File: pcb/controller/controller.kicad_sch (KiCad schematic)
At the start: 0 parts

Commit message: big components placed
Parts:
- added U1: ESP32-H2, PCM_Espressif:QFN-32-1EP_4x4mm_P0.4mm_EP2.9x2.9mm, symbol Espressif:ESP32-H2
- added U2: LSM6DSM, Package_LGA:LGA-14_3x2.5mm_P0.5mm_LayoutBorder3x4y, symbol Sensor_Motion:LSM6DSM
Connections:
- new net: U2.6 (GND), U2.7 (GND)
- new net: U1.1 (VDD3P3), U1.2 (VDD3P3), U1.27 (VDD3P3), U1.30 (VDD3P3), U1.31 (VDD3P3)

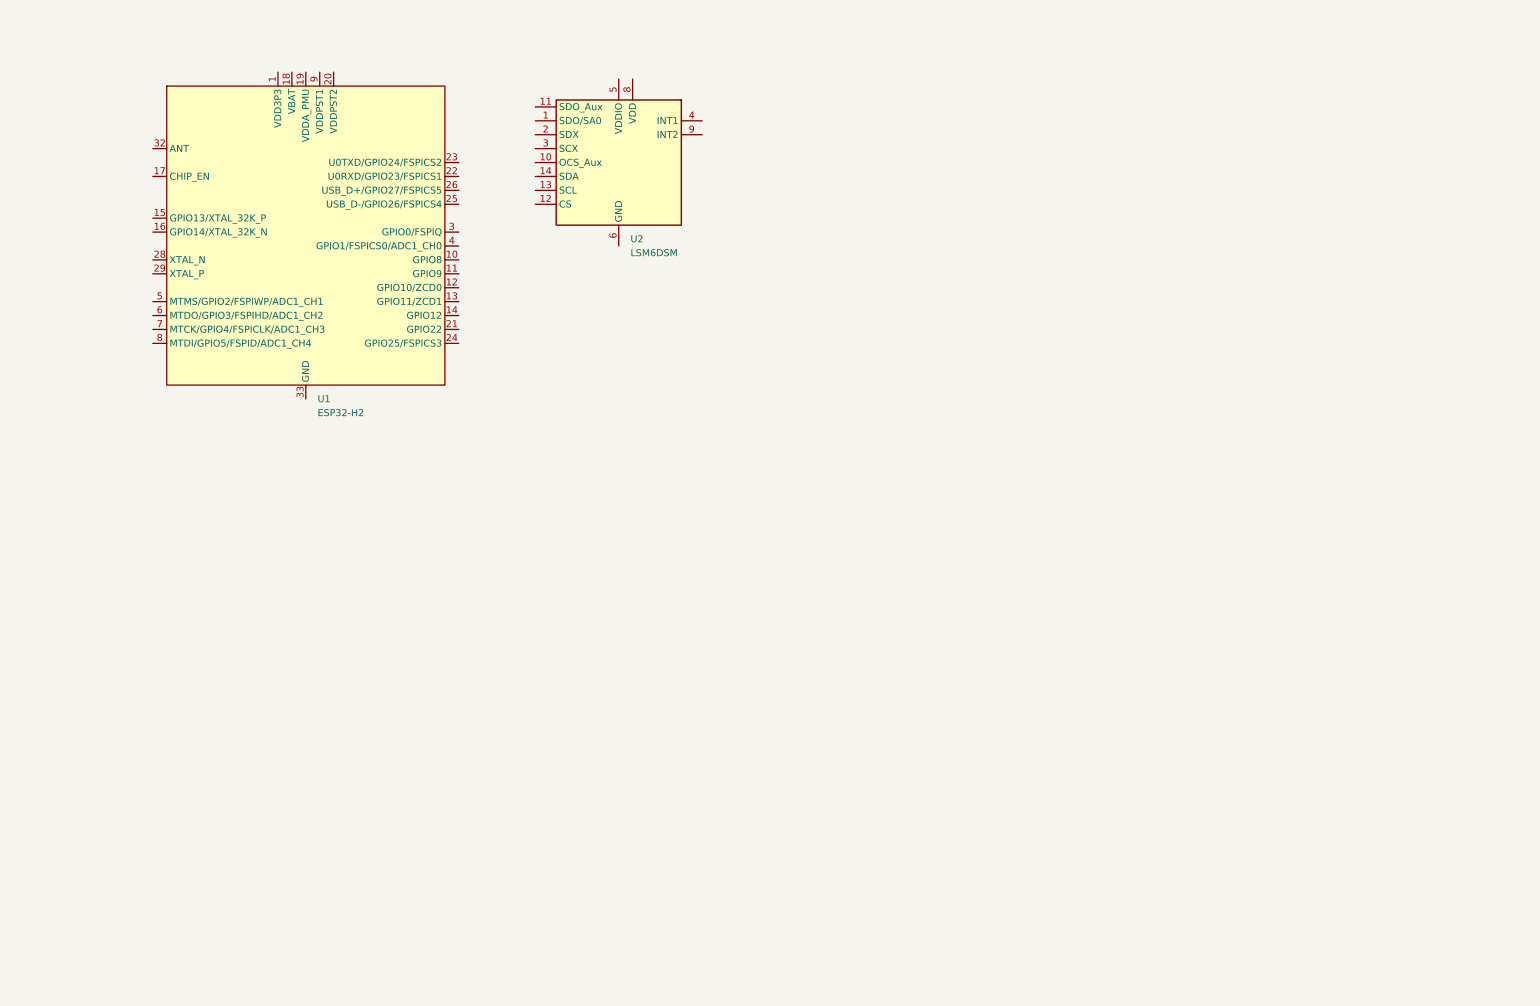
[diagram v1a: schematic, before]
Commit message: copied over wifi board without antenna
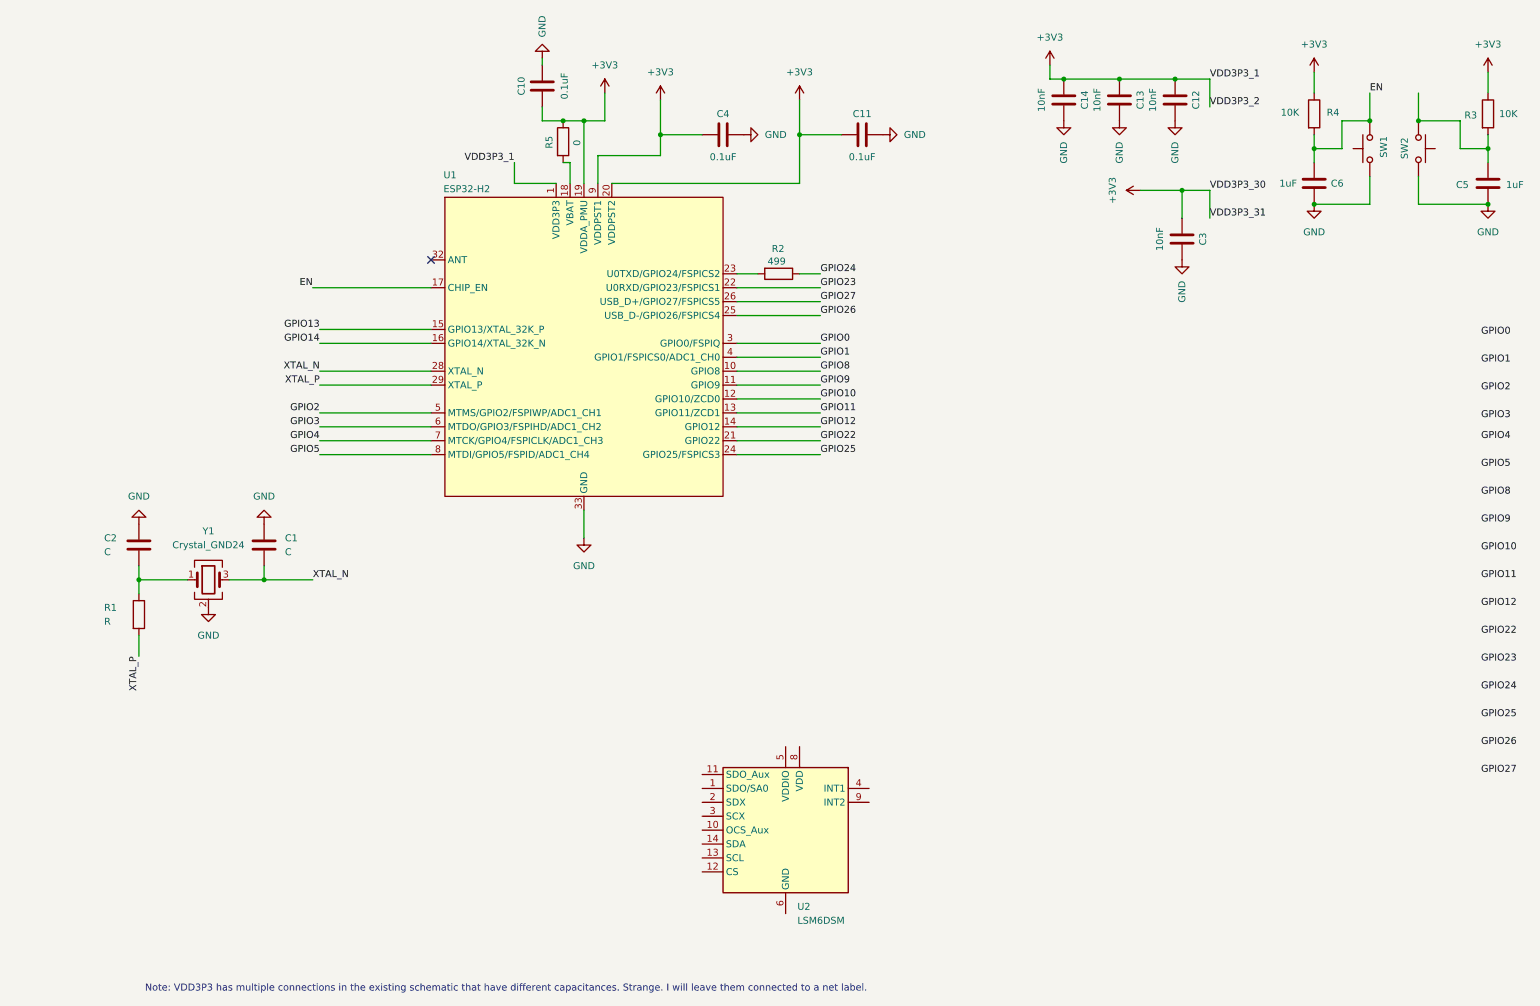
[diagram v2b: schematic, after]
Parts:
- added C1, C2: C, symbol Device:C
- added C10, C11, C4: 0.1uF, symbol Device:C
- added C12, C13, C14, C3: 10nF, symbol Device:C
- added C5, C6: 1uF, symbol Device:C
- added R1: R, symbol Device:R
- added R2: 499, symbol Device:R
- added R3, R4: 10K, symbol Device:R
- added R5: 0, symbol Device:R
- added SW1, SW2: SW_Push, symbol Switch:SW_Push
- added Y1: Crystal_GND24, Crystal:Crystal_SMD_2016-4Pin_2.0x1.6mm, symbol Device:Crystal_GND24
- U1: footprint PCM_Espressif:QFN-32-1EP_4x4mm_P0.4mm_EP2.9x2.9mm -> Espressif:QFN-32-1EP_4x4mm_P0.4mm_EP2.9x2.9mm
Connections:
- net +3V3: now reaches U1.1 (VDD3P3), U1.2 (VDD3P3), U1.27 (VDD3P3), U1.30 (VDD3P3), U1.31 (VDD3P3)
- net +3V3: now also U1.19 (VDDA_PMU), U1.20 (VDDPST2), U1.9 (VDDPST1), C10.2, C11.2, C12.2, C13.2, C14.2, C3.2, C4.2, R3.1, R4.1, R5.1
- net GPIO8: now reaches U1.10 (GPIO8)
- net GPIO9: now reaches U1.11 (GPIO9)
- net GPIO10: now reaches U1.12 (GPIO10/ZCD0)
- net GPIO11: now reaches U1.13 (GPIO11/ZCD1)
- net GPIO12: now reaches U1.14 (GPIO12)
- net GPIO13: now reaches U1.15 (GPIO13/XTAL_32K_P)
- net GPIO14: now reaches U1.16 (GPIO14/XTAL_32K_N)
- net EN: now reaches U1.17 (CHIP_EN)
- net EN: now also C6.1, R4.2, SW1.2
- net at U1.18 (VBAT): now also R5.2
- net GPIO22: now reaches U1.21 (GPIO22)
- net GPIO23: now reaches U1.22 (U0RXD/GPIO23/FSPICS1)
- net at U1.23 (U0TXD/GPIO24/FSPICS2): now also R2.2
- net GPIO25: now reaches U1.24 (GPIO25/FSPICS3)
- net GPIO26: now reaches U1.25 (USB_D-/GPIO26/FSPICS4)
- net GPIO27: now reaches U1.26 (USB_D+/GPIO27/FSPICS5)
- net XTAL_N: now reaches U1.28 (XTAL_N)
- net XTAL_N: now also C1.2, Y1.3
- net XTAL_P: now reaches U1.29 (XTAL_P)
- net XTAL_P: now also R1.2
- net GPIO0: now reaches U1.3 (GPIO0/FSPIQ)
- net GND: now reaches U1.33 (GND)
- net GND: now also C1.1, C10.1, C11.1, C12.1, C13.1, C14.1, C2.1, C3.1, C4.1, C5.2, C6.2, SW1.1, SW2.2, Y1.2 (G), Y1.4 (G)
- net GPIO1: now reaches U1.4 (GPIO1/FSPICS0/ADC1_CH0)
- net GPIO2: now reaches U1.5 (MTMS/GPIO2/FSPIWP/ADC1_CH1)
- net GPIO3: now reaches U1.6 (MTDO/GPIO3/FSPIHD/ADC1_CH2)
- net GPIO4: now reaches U1.7 (MTCK/GPIO4/FSPICLK/ADC1_CH3)
- net GPIO5: now reaches U1.8 (MTDI/GPIO5/FSPID/ADC1_CH4)
- new net: C5.1, R3.2, SW2.1
- new net: C2.2, R1.1, Y1.1
- new net GPIO24: R2.1
- no-connect marks 0 -> 1
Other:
- note added: "Note: VDD3P3 has multiple connections in the existing schematic that have different capacitances. Strange. I will leave them connected to a net label."
- moved on the sheet: U2
